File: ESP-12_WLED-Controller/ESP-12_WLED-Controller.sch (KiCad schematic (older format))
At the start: 24 parts, among them J1 Conn_01x02_Male, J2 Conn_01x04_Male, J3 Conn_01x03_Male, Q1 TSM2302CX, Q2 IRF7410, SW1 SW_RST, U1 TS1117-3.3, U2 ESP-12E, U4 74LVC1G125

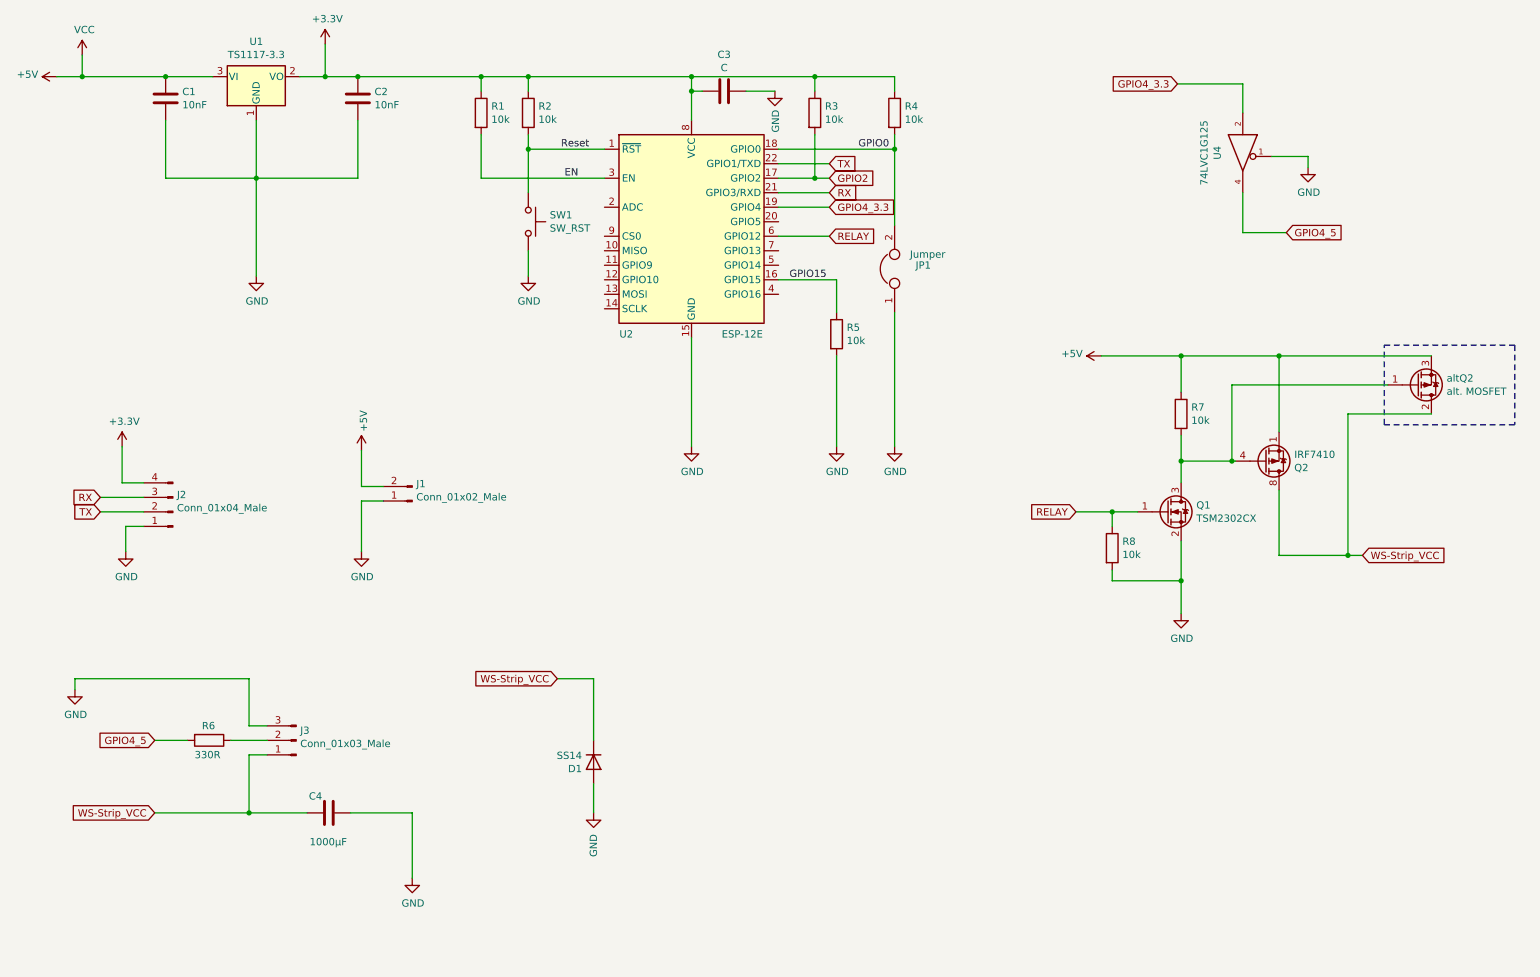
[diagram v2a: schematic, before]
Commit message: some changes
single Terminal-Block
parts clean up
edit footprints for handsolder
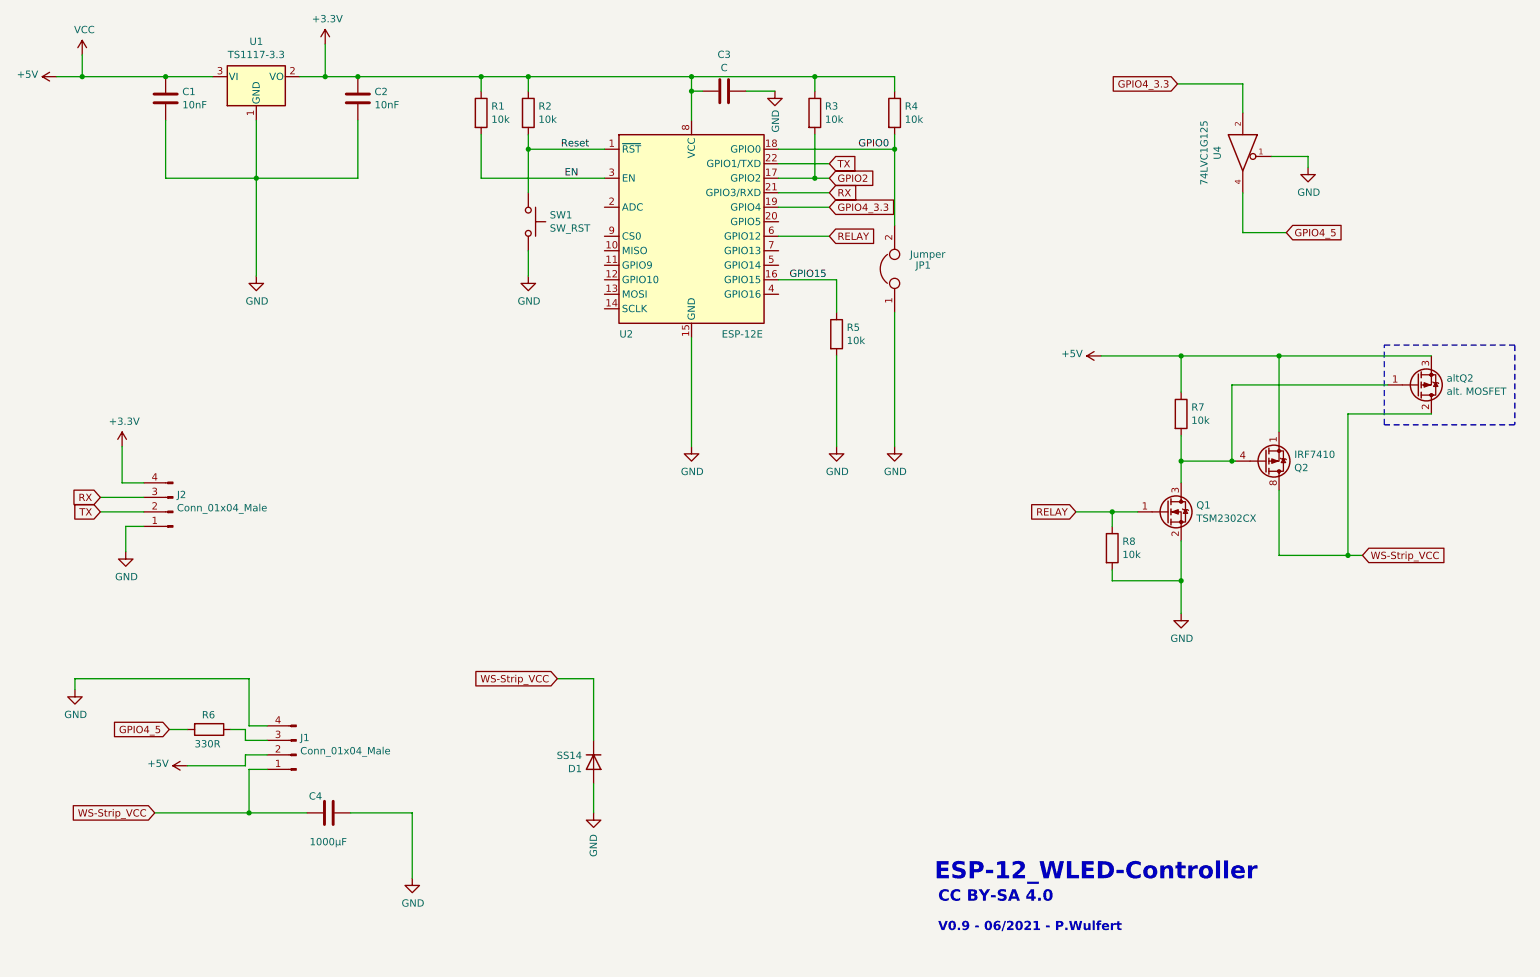
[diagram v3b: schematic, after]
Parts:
- removed J1: Conn_01x02_Male, TerminalBlock_Phoenix:TerminalBlock_Phoenix_MKDS-1,5-2_1x02_P5.00mm_Horizontal, symbol Connector:Conn_01x02_Male
- removed J3: Conn_01x03_Male, TerminalBlock_Phoenix:TerminalBlock_Phoenix_MKDS-1,5-3_1x03_P5.00mm_Horizontal, symbol Connector:Conn_01x03_Male
- added J1: Conn_01x04_Male, TerminalBlock_Phoenix:TerminalBlock_Phoenix_MKDS-1,5-4-5.08_1x04_P5.08mm_Horizontal, symbol Connector:Conn_01x04_Male
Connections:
- net +5V: now also J1.2 (Pin_2)
- net GND: now also J1.4 (Pin_4)
- net WS-Strip_VCC: now also J1.1 (Pin_1)
- net at R6.1: now also J1.3 (Pin_3)
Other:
- note added: "CC BY-SA 4.0"
- note added: "ESP-12_WLED-Controller"
- note added: "V0.9 - 06/2021 - P.Wulfert"
- moved on the sheet: R6
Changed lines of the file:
@@
 Wire Wire Line
 	2275 5675 2400 5675
-Text GLabel 1625 5775 0    50   Input ~ 0
+Text GLabel 1725 5700 0    50   Input ~ 0
 GPIO4_5
-$Comp
-L Connector:Conn_01x02_Male J1
-U 1 1 60CD0E2A
-P 3400 4125
-F 0 "J1" H 3372 4007 50  0000 R CNN
-F 1 "Conn_01x02_Male" H 3372 4098 50  0000 R CNN
-F 2 "TerminalBlock_Phoenix:TerminalBlock_Phoenix_MKDS-1,5-2_1x02_P5.00mm_Horizontal" H 3400 4125 50  0001 C CNN
-F 3 "~" H 3400 4125 50  0001 C CNN
-	1    3400 4125
-	-1   0    0    1
-$EndComp
-$Comp
-L power:+5V #PWR03
-U 1 1 60CD1AA8
-P 3050 3775
-F 0 "#PWR03" H 3050 3625 50  0001 C CNN
-F 1 "+5V" V 3065 3903 50  0000 L CNN
-F 2 "" H 3050 3775 50  0001 C CNN
-F 3 "" H 3050 3775 50  0001 C CNN
-	1    3050 3775
-	1    0    0    -1
-$EndComp
-Wire Wire Line
-	3050 3775 3050 4025
-Wire Wire Line
-	3050 4025 3200 4025
-$Comp
-L power:GND #PWR04
-U 1 1 60CD3285
-P 3050 4475
-F 0 "#PWR04" H 3050 4225 50  0001 C CNN
-F 1 "GND" H 3055 4302 50  0000 C CNN
-F 2 "" H 3050 4475 50  0001 C CNN
-F 3 "" H 3050 4475 50  0001 C CNN
-	1    3050 4475
-	1    0    0    -1
-$EndComp
-Wire Wire Line
-	3050 4475 3050 4125
-Wire Wire Line
-	3050 4125 3200 4125
 $Comp
 L Connector:Conn_01x04_Male J2
@@
 	1    0    0    -1
 $EndComp
-$Comp
-L Connector:Conn_01x03_Male J3
-U 1 1 60CC58BC
-P 2600 5775
-F 0 "J3" H 2572 5707 50  0000 R CNN
-F 1 "Conn_01x03_Male" H 2572 5798 50  0000 R CNN
-F 2 "TerminalBlock_Phoenix:TerminalBlock_Phoenix_MKDS-1,5-3_1x03_P5.00mm_Horizontal" H 2600 5775 50  0001 C CNN
-F 3 "~" H 2600 5775 50  0001 C CNN
-	1    2600 5775
-	-1   0    0    1
-$EndComp
-Wire Wire Line
-	2275 5875 2400 5875
 Wire Wire Line
 	2275 5350 2275 5675
@@
 Wire Wire Line
 	2275 6275 2675 6275
-Wire Wire Line
-	2275 5875 2275 6275
 Connection ~ 2275 6275
 $Comp
@@
 L Device:R R6
 U 1 1 60CE7305
-P 2000 5775
-F 0 "R6" V 1900 5725 50  0000 L CNN
-F 1 "330R" V 2100 5675 50  0000 L CNN
-F 2 "Resistor_SMD:R_0805_2012Metric_Pad1.15x1.40mm_HandSolder" V 1930 5775 50  0001 C CNN
-F 3 "~" H 2000 5775 50  0001 C CNN
-	1    2000 5775
+P 2000 5700
+F 0 "R6" V 1900 5650 50  0000 L CNN
+F 1 "330R" V 2100 5600 50  0000 L CNN
+F 2 "Resistor_SMD:R_0805_2012Metric_Pad1.15x1.40mm_HandSolder" V 1930 5700 50  0001 C CNN
+F 3 "~" H 2000 5700 50  0001 C CNN
+	1    2000 5700
 	0    1    1    0
 $EndComp
 Wire Wire Line
-	1625 5775 1850 5775
+	1725 5700 1850 5700
 Connection ~ 6725 1700
 Wire Wire Line
@@
 	1    0    0    1
 $EndComp
-Wire Wire Line
-	2150 5775 2400 5775
 $Comp
 L Device:D D1
@@
 Wire Wire Line
 	9850 4500 9950 4500
+$Comp
+L Connector:Conn_01x04_Male J1
+U 1 1 60D306B0
+P 2600 5875
+F 0 "J1" H 2572 5757 50  0000 R CNN
+F 1 "Conn_01x04_Male" H 2572 5848 50  0000 R CNN
+F 2 "TerminalBlock_Phoenix:TerminalBlock_Phoenix_MKDS-1,5-4-5.08_1x04_P5.08mm_Horizontal" H 2600 5875 50  0001 C CNN
+F 3 "~" H 2600 5875 50  0001 C CNN
+	1    2600 5875
+	-1   0    0    1
+$EndComp
+Wire Wire Line
+	2400 5975 2275 5975
+Wire Wire Line
+	2275 5975 2275 6275
+Wire Wire Line
+	2150 5700 2250 5700
+Wire Wire Line
+	2250 5700 2250 5775
+Wire Wire Line
+	2250 5775 2400 5775
+$Comp
+L power:+5V #PWR0108
+U 1 1 60D41BF2
+P 1850 5950
+F 0 "#PWR0108" H 1850 5800 50  0001 C CNN
+F 1 "+5V" V 1865 6078 50  0000 L CNN
+F 2 "" H 1850 5950 50  0001 C CNN
+F 3 "" H 1850 5950 50  0001 C CNN
+	1    1850 5950
+	0    -1   -1   0
+$EndComp
+Wire Wire Line
+	1850 5950 2250 5950
+Wire Wire Line
+	2250 5950 2250 5875
+Wire Wire Line
+	2250 5875 2400 5875
+Text Notes 7000 6750 0    118  ~ 24
+ESP-12_WLED-Controller
+Text Notes 7025 6900 0    79   ~ 16
+CC BY-SA 4.0
+Text Notes 7025 7100 0    63   ~ 13
+V0.9 - 06/2021 - P.Wulfert
 $EndSCHEMATC

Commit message: Update to V1.0
clean schematic
add description
TX <-> RX
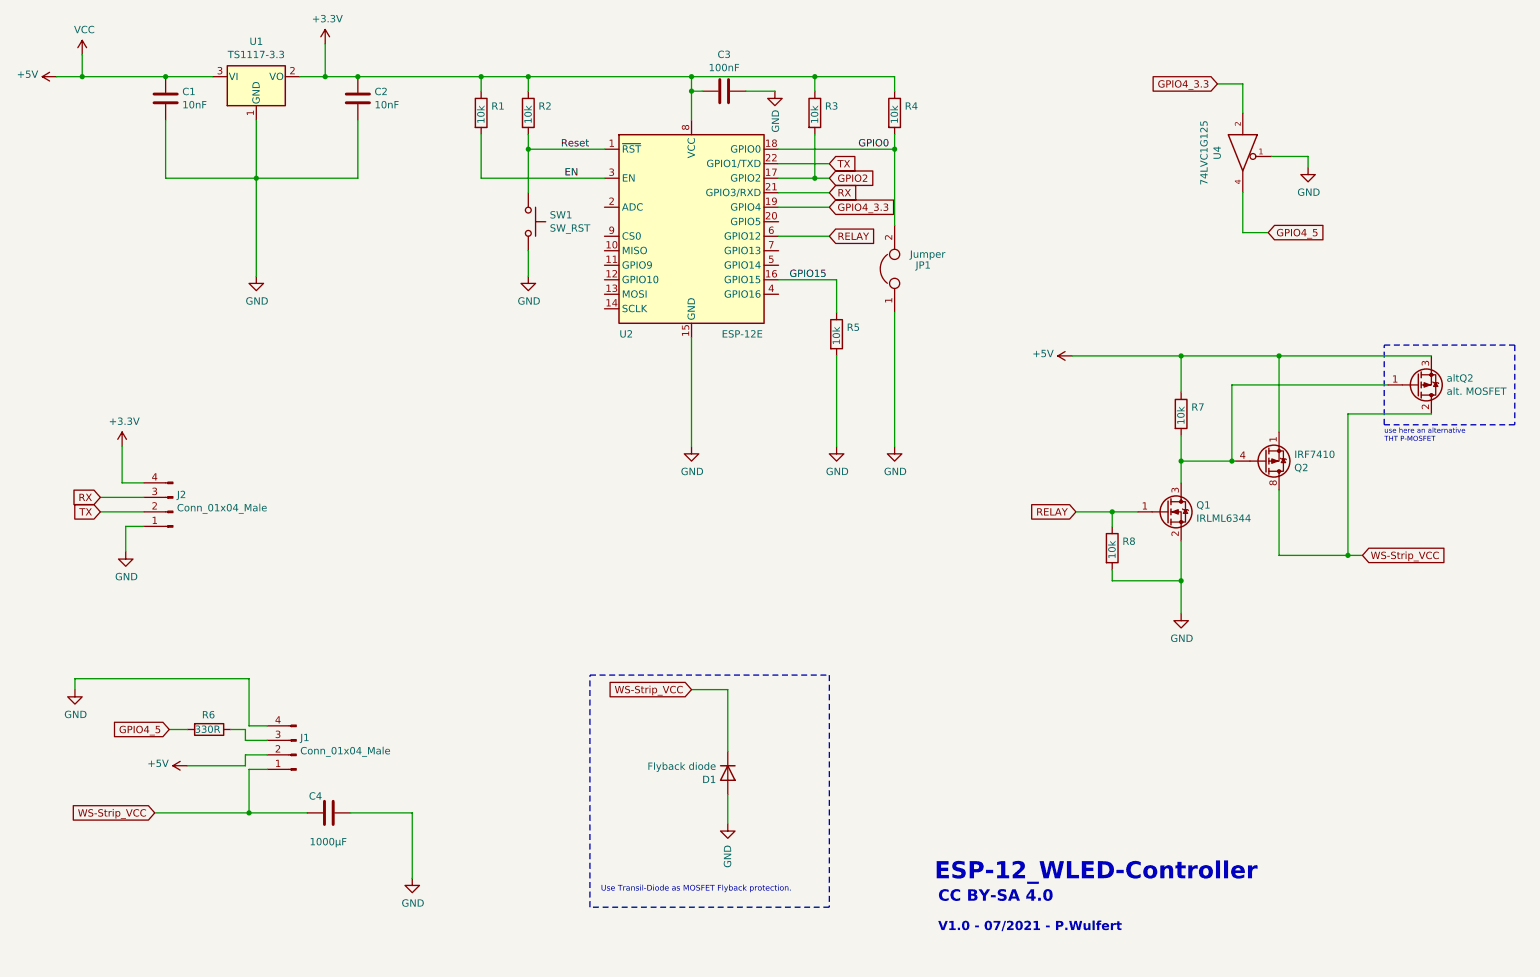
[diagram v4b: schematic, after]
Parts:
- C3: value C -> 100nF
- D1: value SS14 -> Flyback diode
- Q1: value TSM2302CX -> IRLML6344
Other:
- note added: "Use Transil-Diode as MOSFET Flyback protection.\n"
- note added: "V1.0 - 07/2021 - P.Wulfert"
- note added: "use here an alternative \nTHT P-MOSFET"
- note removed: "V0.9 - 06/2021 - P.Wulfert"
- moved on the sheet: D1
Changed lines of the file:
@@
 P 4200 1450
 F 0 "R2" H 4270 1496 50  0000 L CNN
-F 1 "10k" H 4270 1405 50  0000 L CNN
+F 1 "10k" V 4200 1375 50  0000 L CNN
 F 2 "Resistor_SMD:R_0805_2012Metric_Pad1.15x1.40mm_HandSolder" V 4130 1450 50  0001 C CNN
 F 3 "~" H 4200 1450 50  0001 C CNN
@@
 P 3875 1450
 F 0 "R1" H 3945 1496 50  0000 L CNN
-F 1 "10k" H 3945 1405 50  0000 L CNN
+F 1 "10k" V 3875 1375 50  0000 L CNN
 F 2 "Resistor_SMD:R_0805_2012Metric_Pad1.15x1.40mm_HandSolder" V 3805 1450 50  0001 C CNN
 F 3 "~" H 3875 1450 50  0001 C CNN
@@
 P 6725 1450
 F 0 "R4" H 6795 1496 50  0000 L CNN
-F 1 "10k" H 6795 1405 50  0000 L CNN
+F 1 "10k" V 6725 1375 50  0000 L CNN
 F 2 "Resistor_SMD:R_0805_2012Metric_Pad1.15x1.40mm_HandSolder" V 6655 1450 50  0001 C CNN
 F 3 "~" H 6725 1450 50  0001 C CNN
@@
 P 5550 1300
 F 0 "C3" V 5298 1300 50  0000 C CNN
-F 1 "C" V 5389 1300 50  0000 C CNN
+F 1 "100nF" V 5389 1300 50  0000 C CNN
 F 2 "Capacitor_SMD:C_0805_2012Metric_Pad1.15x1.40mm_HandSolder" H 5588 1150 50  0001 C CNN
 F 3 "~" H 5550 1300 50  0001 C CNN
@@
 P 6175 1450
 F 0 "R3" H 6245 1496 50  0000 L CNN
-F 1 "10k" H 6245 1405 50  0000 L CNN
+F 1 "10k" V 6175 1375 50  0000 L CNN
 F 2 "Resistor_SMD:R_0805_2012Metric_Pad1.15x1.40mm_HandSolder" V 6105 1450 50  0001 C CNN
 F 3 "~" H 6175 1450 50  0001 C CNN
@@
 P 6325 2975
 F 0 "R5" H 6395 3021 50  0000 L CNN
-F 1 "10k" H 6395 2930 50  0000 L CNN
+F 1 "10k" V 6325 2900 50  0000 L CNN
 F 2 "Resistor_SMD:R_0805_2012Metric_Pad1.15x1.40mm_HandSolder" V 6255 2975 50  0001 C CNN
 F 3 "~" H 6325 2975 50  0001 C CNN
@@
 P 2000 5700
 F 0 "R6" V 1900 5650 50  0000 L CNN
-F 1 "330R" V 2100 5600 50  0000 L CNN
+F 1 "330R" V 2000 5600 50  0000 L CNN
 F 2 "Resistor_SMD:R_0805_2012Metric_Pad1.15x1.40mm_HandSolder" V 1930 5700 50  0001 C CNN
 F 3 "~" H 2000 5700 50  0001 C CNN
@@
 P 8700 3525
 F 0 "R7" H 8770 3571 50  0000 L CNN
-F 1 "10k" H 8770 3480 50  0000 L CNN
+F 1 "10k" V 8700 3450 50  0000 L CNN
 F 2 "Resistor_SMD:R_0805_2012Metric_Pad1.15x1.40mm_HandSolder" V 8630 3525 50  0001 C CNN
 F 3 "~" H 8700 3525 50  0001 C CNN
@@
 L power:+5V #PWR0103
 U 1 1 60D1C6F6
-P 8150 3125
-F 0 "#PWR0103" H 8150 2975 50  0001 C CNN
-F 1 "+5V" V 8165 3253 50  0000 L CNN
-F 2 "" H 8150 3125 50  0001 C CNN
-F 3 "" H 8150 3125 50  0001 C CNN
-	1    8150 3125
+P 7950 3125
+F 0 "#PWR0103" H 7950 2975 50  0001 C CNN
+F 1 "+5V" V 7965 3253 50  0000 L CNN
+F 2 "" H 7950 3125 50  0001 C CNN
+F 3 "" H 7950 3125 50  0001 C CNN
+	1    7950 3125
 	0    -1   -1   0
 $EndComp
 Wire Wire Line
-	8150 3125 8700 3125
+	7950 3125 8700 3125
 Wire Wire Line
 	8700 3375 8700 3125
@@
 F 1 "IRF7410" H 9480 3805 50  0000 L CNN
 F 2 "Package_SO:SOIC-8_3.9x4.9mm_P1.27mm" H 9475 3775 50  0001 L CIN
-F 3 "http://www.infineon.com/dgdl/irf7404.pdf?fileId=5546d462533600a4015355fa2b5b1b9e" V 9275 3850 50  0001 L CNN
+F 3 "https://cdn-reichelt.de/documents/datenblatt/A200/DS_IRF7410.pdf" V 9275 3850 50  0001 L CNN
 	1    9275 3850
 	1    0    0    1
@@
 L Device:D D1
 U 1 1 60D1AEEC
-P 4650 5925
-F 0 "D1" V 4696 5845 50  0000 R CNN
-F 1 "SS14" V 4605 5845 50  0000 R CNN
-F 2 "Diode_SMD:D_SMA_Handsoldering" H 4650 5925 50  0001 C CNN
-F 3 "~" H 4650 5925 50  0001 C CNN
-	1    4650 5925
+P 5575 6000
+F 0 "D1" V 5621 5920 50  0000 R CNN
+F 1 "Flyback diode" V 5530 5920 50  0000 R CNN
+F 2 "Diode_SMD:D_SMA_Handsoldering" H 5575 6000 50  0001 C CNN
+F 3 "~" H 5575 6000 50  0001 C CNN
+	1    5575 6000
 	0    1    1    0
 $EndComp
@@
 L power:GND #PWR014
 U 1 1 60CC9228
-P 4650 6275
-F 0 "#PWR014" H 4650 6025 50  0001 C CNN
-F 1 "GND" V 4650 6050 50  0000 C CNN
-F 2 "" H 4650 6275 50  0001 C CNN
-F 3 "" H 4650 6275 50  0001 C CNN
-	1    4650 6275
+P 5575 6350
+F 0 "#PWR014" H 5575 6100 50  0001 C CNN
+F 1 "GND" V 5575 6125 50  0000 C CNN
+F 2 "" H 5575 6350 50  0001 C CNN
+F 3 "" H 5575 6350 50  0001 C CNN
+	1    5575 6350
 	1    0    0    -1
 $EndComp
@@
 	9050 3850 9075 3850
 Connection ~ 9375 3125
-Text GLabel 4400 5350 0    50   Input ~ 0
+Text GLabel 5325 5425 0    50   Input ~ 0
 WS-Strip_VCC
 Wire Wire Line
-	4650 6275 4650 6075
-Wire Wire Line
-	4400 5350 4650 5350
-Wire Wire Line
-	4650 5350 4650 5775
+	5575 6350 5575 6150
+Wire Wire Line
+	5325 5425 5575 5425
+Wire Wire Line
+	5575 5425 5575 5850
 Wire Wire Line
 	1625 6275 2275 6275
@@
 Wire Notes Line
 	10100 3600 10100 3050
-Text GLabel 8675 1250 0    50   Input ~ 0
+Text GLabel 8950 1250 0    50   Input ~ 0
 GPIO4_3.3
-Text GLabel 9425 2275 2    50   Input ~ 0
+Text GLabel 9300 2275 2    50   Input ~ 0
 GPIO4_5
 $Comp
@@
 $EndComp
 Wire Wire Line
-	9425 2275 9125 2275
+	9300 2275 9125 2275
 Wire Wire Line
 	9125 2275 9125 2000
 Wire Wire Line
-	8675 1250 9125 1250
+	8950 1250 9125 1250
 Wire Wire Line
 	9125 1250 9125 1450
@@
 P 8600 4200
 F 0 "Q1" H 8805 4246 50  0000 L CNN
-F 1 "TSM2302CX" H 8805 4155 50  0000 L CNN
+F 1 "IRLML6344" H 8805 4155 50  0000 L CNN
 F 2 "Package_TO_SOT_SMD:SOT-23" H 8800 4125 50  0001 L CIN
-F 3 "https://www.taiwansemi.com/products/datasheet/TSM2302CX_E1608.pdf" H 8600 4200 50  0001 L CNN
+F 3 "https://cdn-reichelt.de/documents/datenblatt/A200/DS_IRLML6344-IR.pdf" H 8600 4200 50  0001 L CNN
 	1    8600 4200
 	1    0    0    -1
@@
 P 8225 4450
 F 0 "R8" H 8295 4496 50  0000 L CNN
-F 1 "10k" H 8295 4405 50  0000 L CNN
+F 1 "10k" V 8225 4375 50  0000 L CNN
 F 2 "Resistor_SMD:R_0805_2012Metric_Pad1.15x1.40mm_HandSolder" V 8155 4450 50  0001 C CNN
 F 3 "~" H 8225 4450 50  0001 C CNN
@@
 CC BY-SA 4.0
 Text Notes 7025 7100 0    63   ~ 13
-V0.9 - 06/2021 - P.Wulfert
+V1.0 - 07/2021 - P.Wulfert
+Text Notes 10100 3725 0    35   ~ 0
+use here an alternative \nTHT P-MOSFET
+Wire Notes Line
+	4625 5325 6275 5325
+Wire Notes Line
+	6275 5325 6275 6925
+Wire Notes Line
+	6275 6925 4625 6925
+Wire Notes Line
+	4625 6925 4625 5325
+Text Notes 4700 6825 0    39   ~ 0
+Use Transil-Diode as MOSFET Flyback protection.\n
 $EndSCHEMATC

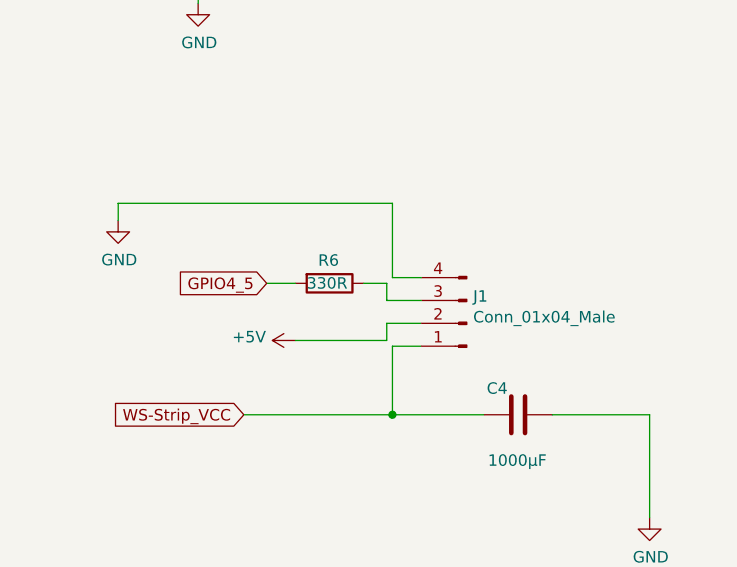
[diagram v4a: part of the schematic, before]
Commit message: update schematic
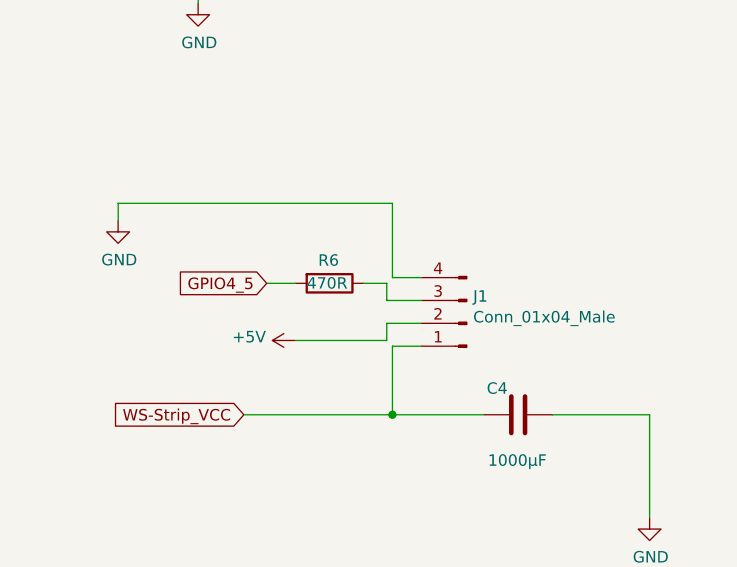
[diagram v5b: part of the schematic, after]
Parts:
- R6: value 330R -> 470R
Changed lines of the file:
@@
 P 2000 5700
 F 0 "R6" V 1900 5650 50  0000 L CNN
-F 1 "330R" V 2000 5600 50  0000 L CNN
+F 1 "470R" V 2000 5600 50  0000 L CNN
 F 2 "Resistor_SMD:R_0805_2012Metric_Pad1.15x1.40mm_HandSolder" V 1930 5700 50  0001 C CNN
 F 3 "~" H 2000 5700 50  0001 C CNN

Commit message: V 1.01
update schematic to 1.01
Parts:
- C1, C2: value 10nF -> 10µF
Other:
- note added: "V1.01 - 11/2021 - P.Wulfert"
- note removed: "V1.0 - 07/2021 - P.Wulfert"
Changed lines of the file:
@@
 P 1700 1350
 F 0 "C1" H 1815 1396 50  0000 L CNN
-F 1 "10nF" H 1815 1305 50  0000 L CNN
+F 1 "10µF" H 1815 1305 50  0000 L CNN
 F 2 "Capacitor_SMD:C_0805_2012Metric_Pad1.15x1.40mm_HandSolder" H 1738 1200 50  0001 C CNN
 F 3 "~" H 1700 1350 50  0001 C CNN
@@
 P 3025 1350
 F 0 "C2" H 3140 1396 50  0000 L CNN
-F 1 "10nF" H 3140 1305 50  0000 L CNN
+F 1 "10µF" H 3140 1305 50  0000 L CNN
 F 2 "Capacitor_SMD:C_0805_2012Metric_Pad1.15x1.40mm_HandSolder" H 3063 1200 50  0001 C CNN
 F 3 "~" H 3025 1350 50  0001 C CNN
@@
 CC BY-SA 4.0
 Text Notes 7025 7100 0    63   ~ 13
-V1.0 - 07/2021 - P.Wulfert
+V1.01 - 11/2021 - P.Wulfert
 Text Notes 10100 3725 0    35   ~ 0
 use here an alternative \nTHT P-MOSFET
